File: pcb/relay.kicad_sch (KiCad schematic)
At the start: 17 parts, among them K1 PR24-5V-900-1A, P1 MountingHole_Pad, P2 MountingHole_Pad, P3 MountingHole_Pad, P4 MountingHole_Pad, Q1 MMBT3904, U3 LTV-356T

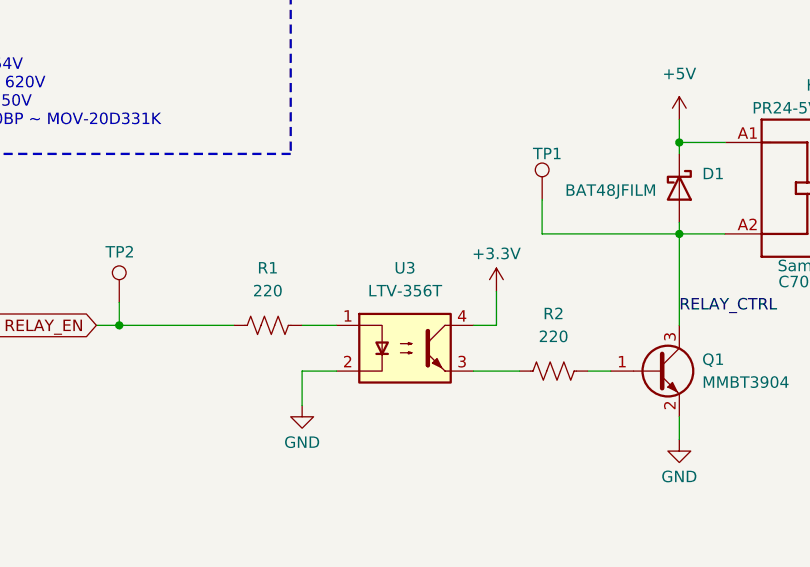
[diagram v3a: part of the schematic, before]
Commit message: Updated I2C pulls to open jumper
Fixed I2C to be open rather than bridged.
Changed opto-isolator to CRGM library.
Updated picture of bottom side to match new footprint
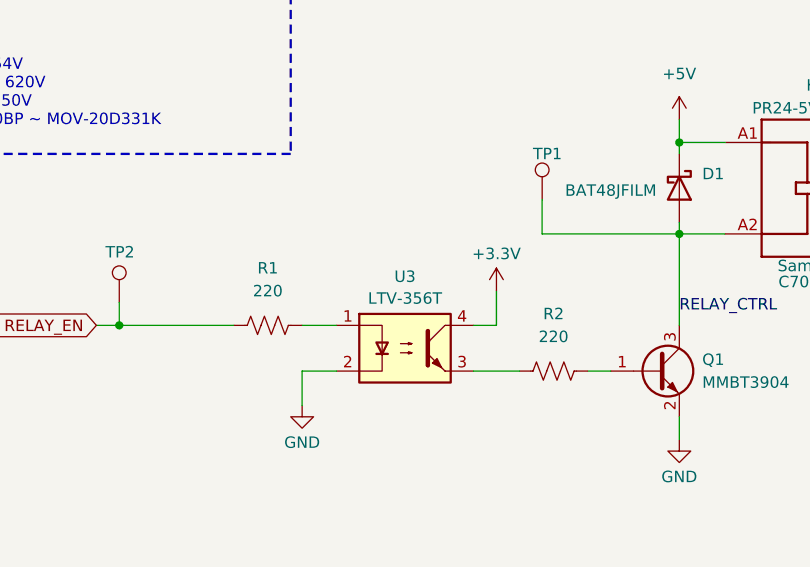
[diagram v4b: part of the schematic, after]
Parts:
- TP1, TP2: now left out of the parts list
- U3: footprint Package_SO:SO-4_4.4x3.6mm_P2.54mm -> CRG Makes:SO-4_4.4x3.6mm_P2.54mm; symbol Isolator:LTV-356T -> CRG Makes:LTV-356T
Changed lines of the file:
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@@
+			)
+		)
+		(property "Sim.Enable" ""
+			(at 162.56 77.47 0)
+			(effects
+				(font
+					(size 1.27 1.27)
+				)
+				(hide yes)
 			)
 		)
@@
 			)
 		)
+		(property "Sim.Enable" ""
+			(at 148.59 40.64 90)
+			(effects
+				(font
+					(size 1.27 1.27)
+				)
+				(hide yes)
+			)
+		)
 		(pin "1"
 		)
@@
 					(size 1.27 1.27)
 				)
+			)
+		)
+		(property "Sim.Enable" ""
+			(at 118.11 45.72 0)
+			(effects
+				(font
+					(size 1.27 1.27)
+				)
+				(hide yes)
 			)
 		)
@@
 	)
 	(symbol
-		(lib_id "Isolator:LTV-356T")
+		(lib_id "CRG Makes:LTV-356T")
 		(at 72.39 63.5 0)
 		(unit 1)
@@
 		(fields_autoplaced yes)
 		(property "Reference" "U3"
-			(at 72.39 54.61 0)
+			(at 72.39 55.5455 0)
 			(effects
 				(font
@@
 		)
 		(property "Value" "LTV-356T"
-			(at 72.39 57.15 0)
-			(effects
-				(font
-					(size 1.27 1.27)
-				)
-			)
-		)
-		(property "Footprint" "Package_SO:SO-4_4.4x3.6mm_P2.54mm"
-			(at 67.31 68.58 0)
+			(at 72.39 57.9698 0)
+			(effects
+				(font
+					(size 1.27 1.27)
+				)
+			)
+		)
+		(property "Footprint" "CRG Makes:SO-4_4.4x3.6mm_P2.54mm"
+			(at 54.356 75.692 0)
 			(effects
 				(font
@@
 		)
 		(property "Datasheet" "http://optoelectronics.liteon.com/upload/download/DS70-2001-010/S_110_LTV-356T%2020140520.pdf"
-			(at 72.39 63.5 0)
+			(at 49.276 72.136 0)
 			(effects
 				(font
@@
 		)
 		(property "Description" "DC Optocoupler, Vce 80V, CTR 50%, SO-4"
-			(at 72.39 63.5 0)
+			(at 72.136 69.342 0)
 			(effects
 				(font
@@
 		)
 		(property "MN" "Lite-On"
+			(at 72.39 63.5 0)
+			(effects
+				(font
+					(size 1.27 1.27)
+				)
+				(hide yes)
+			)
+		)
+		(property "Sim.Enable" ""
 			(at 72.39 63.5 0)
 			(effects
@@
 			)
 		)
+		(property "Sim.Enable" ""
+			(at 135.89 57.15 0)
+			(effects
+				(font
+					(size 1.27 1.27)
+				)
+				(hide yes)
+			)
+		)
 		(pin "P$1"
 		)
@@
 		(unit 1)
 		(exclude_from_sim no)
-		(in_bom yes)
+		(in_bom no)
 		(on_board yes)
 		(dnp no)
@@
 		(property "Description" "Test Point D1.0mm"
 			(at 40.64 67.564 0)
+			(effects
+				(font
+					(size 1.27 1.27)
+				)
+				(hide yes)
+			)
+		)
+		(property "Sim.Enable" ""
+			(at 40.64 58.42 0)
 			(effects
 				(font
@@
 			)
 		)
+		(property "Sim.Enable" ""
+			(at 27.94 114.3 0)
+			(effects
+				(font
+					(size 1.27 1.27)
+				)
+				(hide yes)
+			)
+		)
 		(pin "2"
 		)
@@
 			)
 		)
+		(property "Sim.Enable" ""
+			(at 148.59 48.26 90)
+			(effects
+				(font
+					(size 1.27 1.27)
+				)
+				(hide yes)
+			)
+		)
 		(pin "1"
 		)
@@
 					(size 1 1)
 					(color 223 129 255 1)
+				)
+				(hide yes)
+			)
+		)
+		(property "Sim.Enable" ""
+			(at 22.86 102.87 0)
+			(effects
+				(font
+					(size 1.27 1.27)
 				)
 				(hide yes)
@@
 			)
 		)
+		(property "Sim.Enable" ""
+			(at 57.15 60.96 90)
+			(effects
+				(font
+					(size 1.27 1.27)
+				)
+				(hide yes)
+			)
+		)
 		(pin "2"
 		)
@@
 			)
 		)
+		(property "Sim.Enable" ""
+			(at 100.33 66.04 0)
+			(effects
+				(font
+					(size 1.27 1.27)
+				)
+				(hide yes)
+			)
+		)
 		(pin "3"
 		)
@@
 		(property "MN" "STMicroelectronics"
 			(at 102.87 45.72 0)
+			(effects
+				(font
+					(size 1.27 1.27)
+				)
+				(hide yes)
+			)
+		)
+		(property "Sim.Enable" ""
+			(at 102.87 45.72 90)
 			(effects
 				(font
@@
 			)
 		)
+		(property "Sim.Enable" ""
+			(at 88.9 66.04 90)
+			(effects
+				(font
+					(size 1.27 1.27)
+				)
+				(hide yes)
+			)
+		)
 		(pin "2"
 		)
@@
 			)
 		)
+		(property "Sim.Enable" ""
+			(at 127 66.04 90)
+			(effects
+				(font
+					(size 1.27 1.27)
+				)
+				(hide yes)
+			)
+		)
 		(pin "1"
 		)
@@
 			)
 		)
+		(property "Sim.Enable" ""
+			(at 144.78 66.04 90)
+			(effects
+				(font
+					(size 1.27 1.27)
+				)
+				(hide yes)
+			)
+		)
 		(pin "1"
 		)
@@
 			)
 		)
+		(property "Sim.Enable" ""
+			(at 22.86 109.22 90)
+			(effects
+				(font
+					(size 1.27 1.27)
+				)
+				(hide yes)
+			)
+		)
 		(pin "1"
 		)
@@
 		(unit 1)
 		(exclude_from_sim no)
-		(in_bom yes)
+		(in_bom no)
 		(on_board yes)
 		(dnp no)
@@
 			(effects
 				(font
+					(size 1.27 1.27)
+				)
+				(hide yes)
+			)
+		)
+		(property "Sim.Enable" ""
+			(at 87.63 46.99 0)
+			(effects
+				(font
